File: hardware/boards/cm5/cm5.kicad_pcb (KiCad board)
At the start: 6 copper layers, 64.2 x 85.8 mm, 77 parts, among them J101 10164227-1001A1RLF, J102 10164227-1001A1RLF, J103 BM04B-SRSS-TB, J201 05A20L24P, J401 1054500101, J501 USB4105-GF-A-120, J601 HR911130A, J701 1-2199230-5, M1 CM5, Q401 2N7002, SW501 SKRTLAE010, U301 LM61480RPHR, U401 HD3SS3220RNHR, U402 AP22652W6-7, U403 TPD4E02B04DQAR, U404 TPD4E02B04DQAR, U405 TPD4E05U06DQAR, U501 TPD4E05U06DQAR, U601 TPD4E02B04DQAR, U602 TPD4E02B04DQAR, U701 AP3441SHE-7B

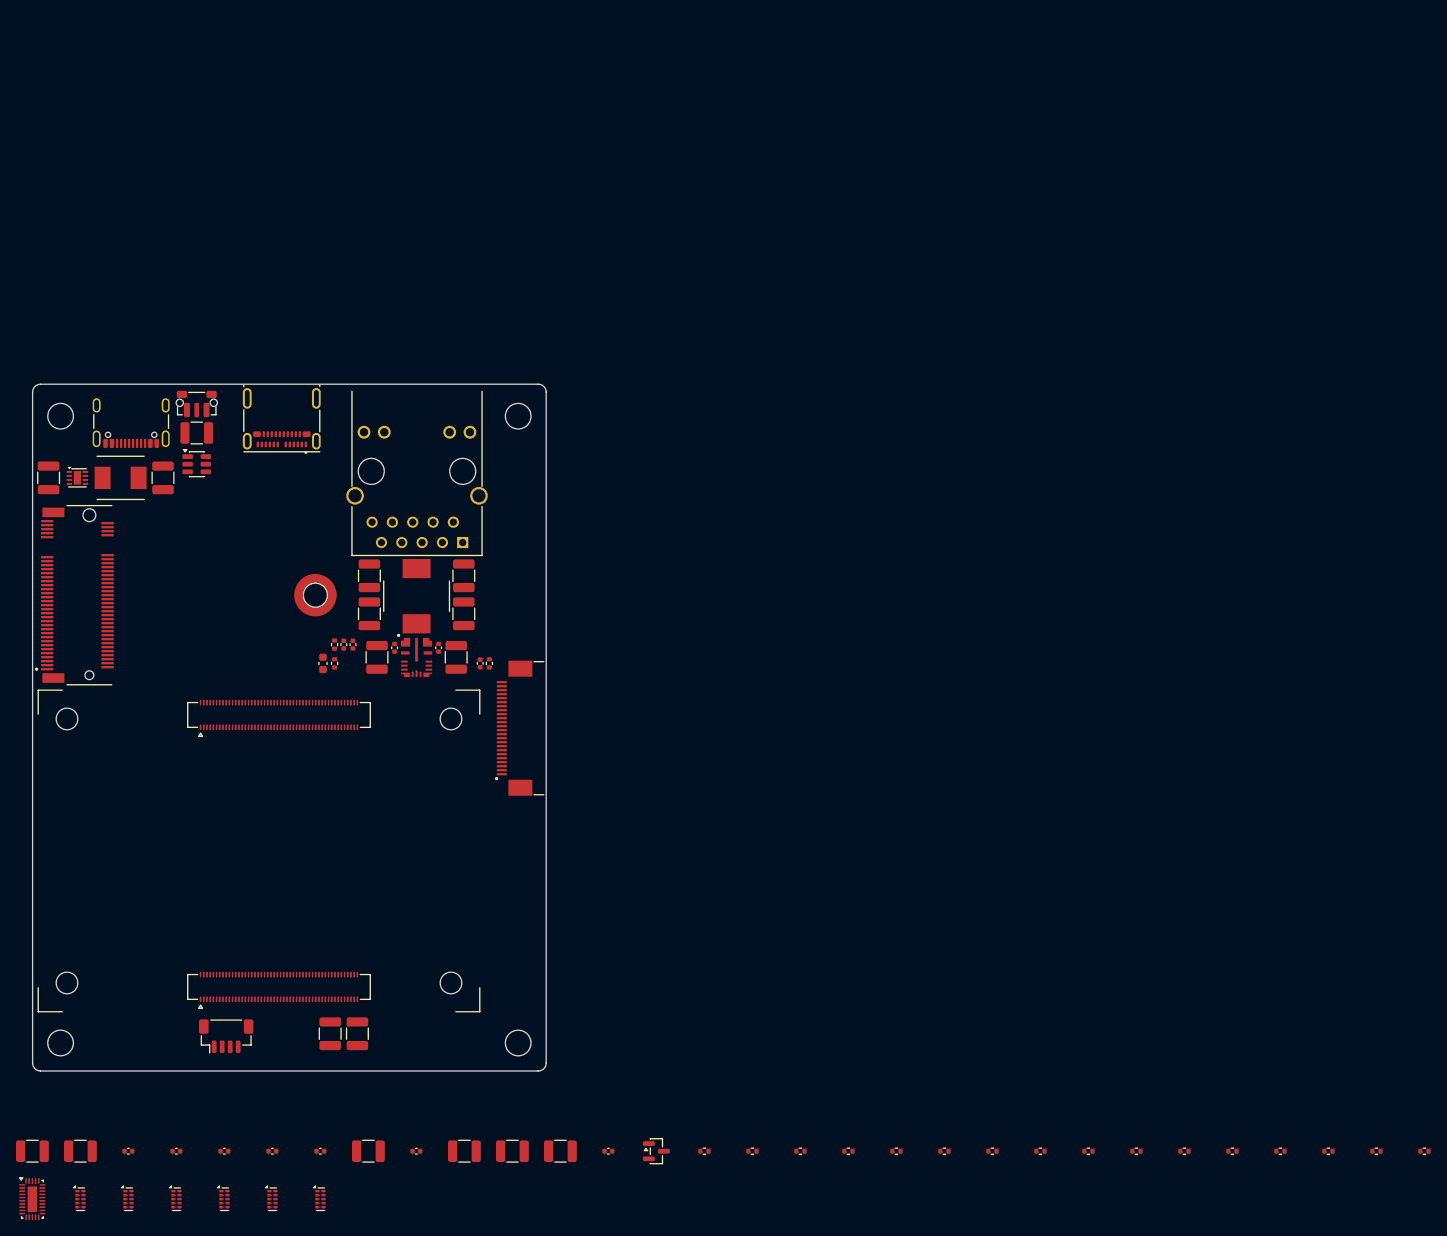
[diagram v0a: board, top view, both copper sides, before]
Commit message: feat(cm5): place the side board around a 2280 beside the turned CM5
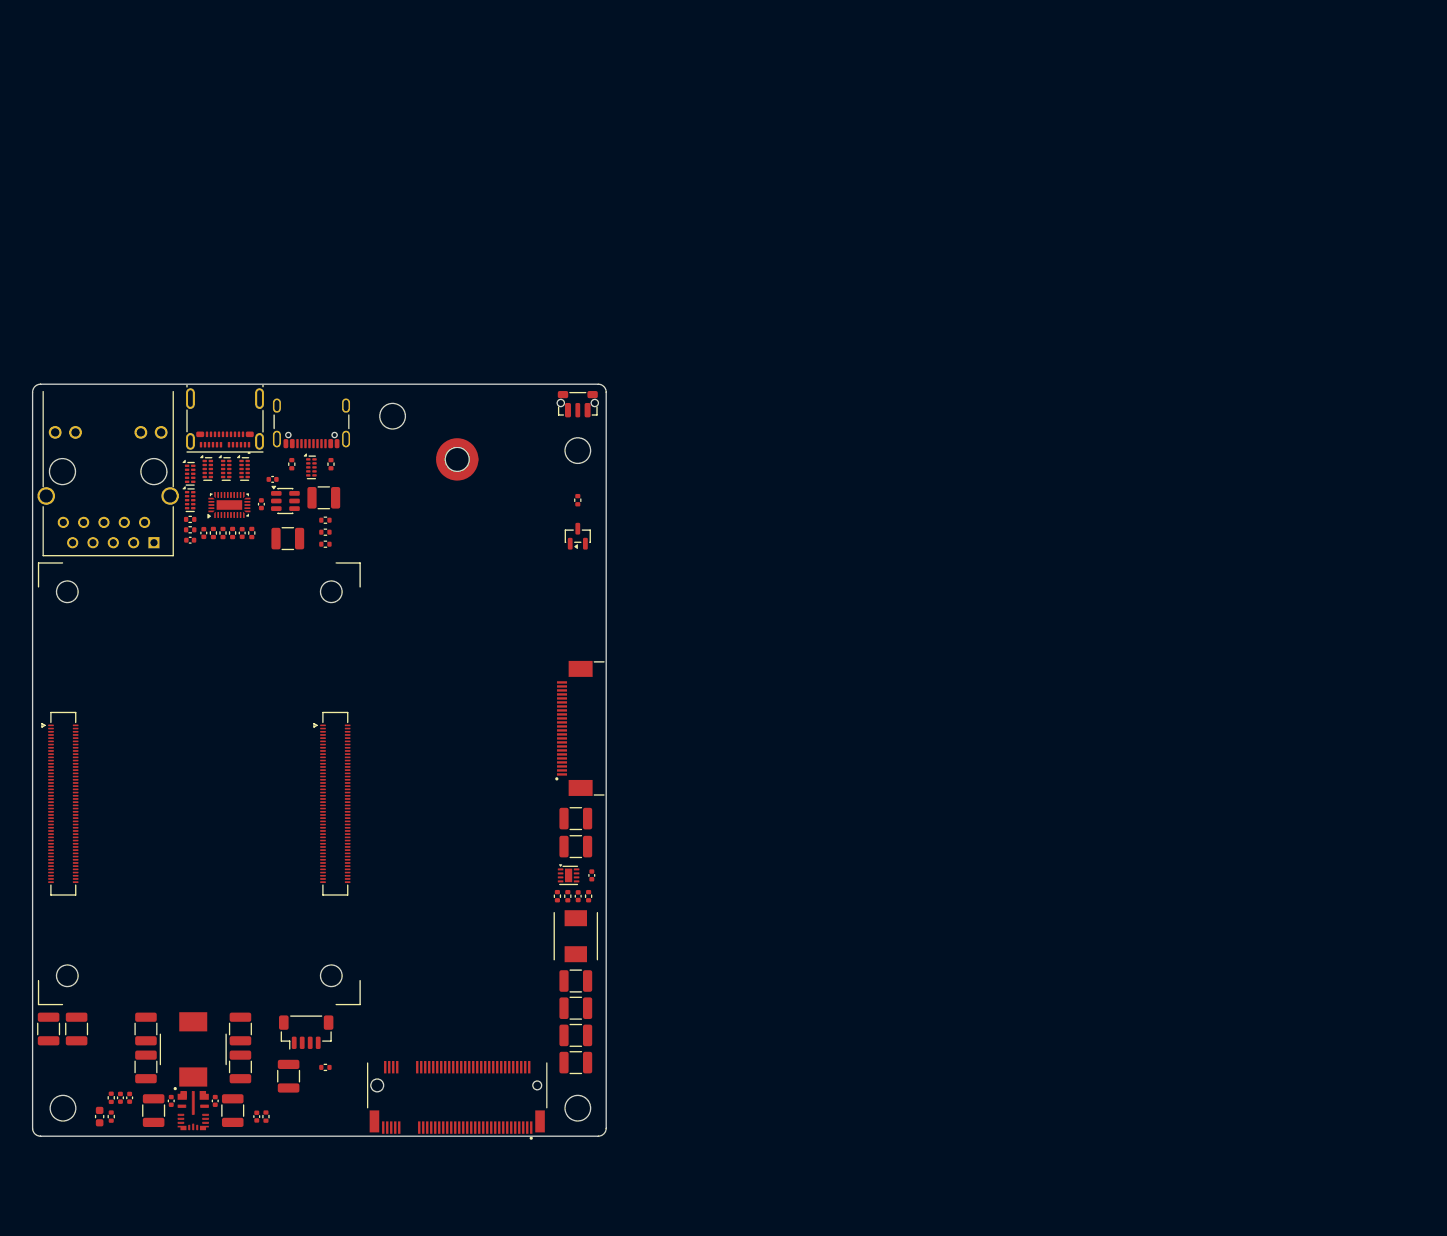
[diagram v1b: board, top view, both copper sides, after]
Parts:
- moved R602 156.9 mm to (119.7, 118.2)
- moved R601 152.3 mm to (119.7, 116.9)
- moved R502 140.8 mm to (132.4, 110.0), turned to 90 degrees
- moved R501 132.3 mm to (137.3, 110.0), turned to 90 degrees
- moved R407 123.8 mm to (136.6, 117.0)
- moved R406 117.2 mm to (136.6, 120.0)
- moved R404 116.0 mm to (127.4, 118.6), turned to 90 degrees
- moved R405 113.7 mm to (136.6, 118.5)
- moved R403 113.4 mm to (125.0, 118.6), turned to 90 degrees
- moved R402 109.9 mm to (123.8, 118.6), turned to 90 degrees
- moved R703 109.2 mm to (169.5, 164.0), turned to 90 degrees
- moved R401 106.6 mm to (122.6, 118.6), turned to 90 degrees
- moved R702 106.0 mm to (166.9, 164.0), turned to 90 degrees
- moved R701 101.5 mm to (165.6, 164.0), turned to 90 degrees
- moved U403 93.6 mm to (126.5, 110.6)
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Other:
- board size 64.2 x 85.8 mm -> 71.7 x 94 mm

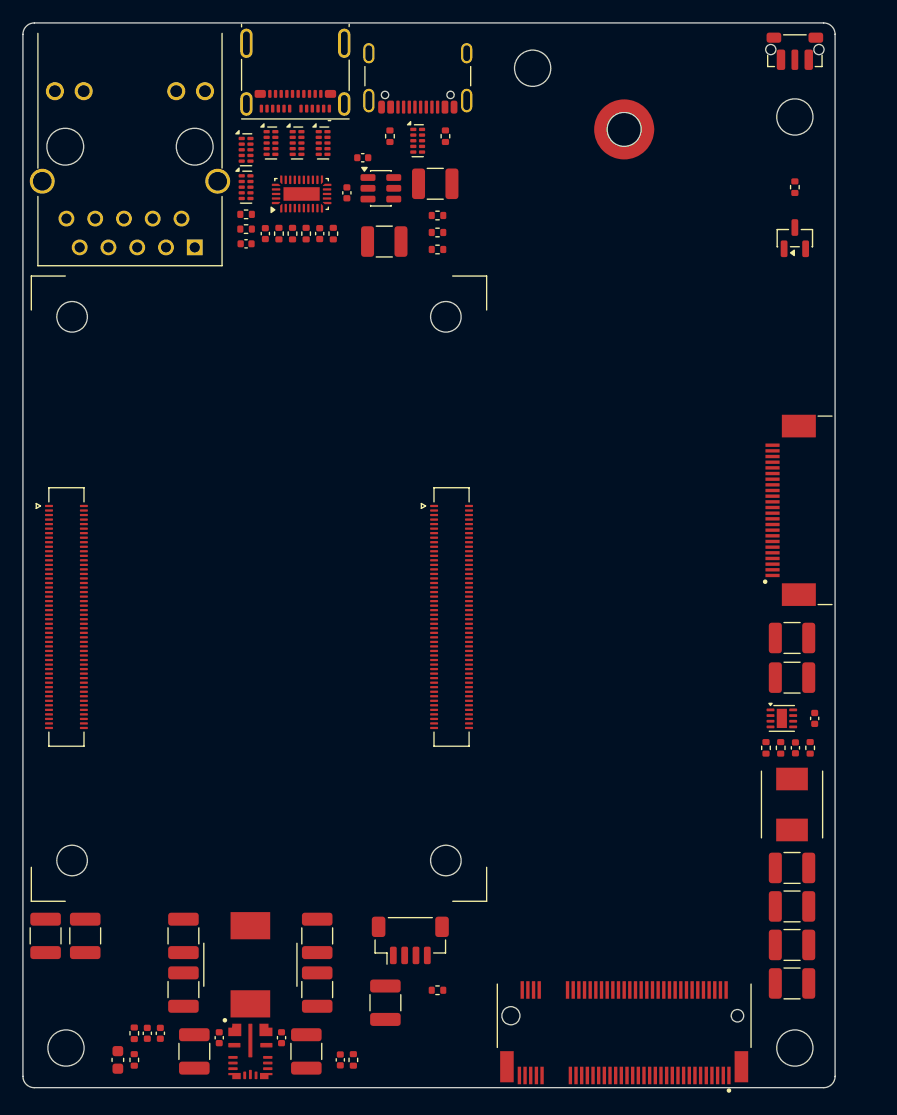
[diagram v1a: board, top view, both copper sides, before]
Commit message: feat(cm5): widen the side board for the CM5 enclosure
The contents move 3.4 mm right so the enclosure's end clip and its travel stop clear the cooler, the RJ45 and C101/C102 at the left edge. The corners take the main board's 3 mm radius, SW501 moves 1 mm in from the rear-right arc, and J501 0.1 mm toward the rear edge so the rear wall keeps 1.0 mm.
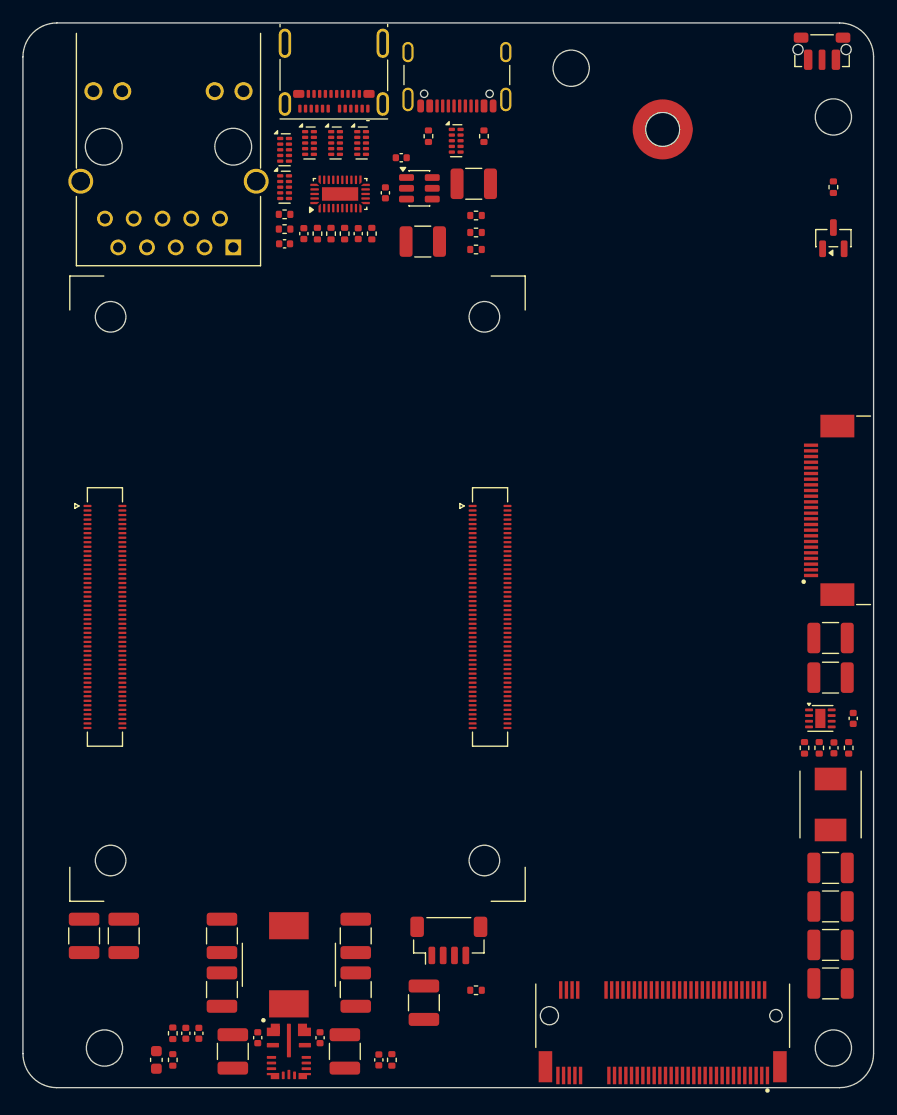
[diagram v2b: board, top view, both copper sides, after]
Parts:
- moved J501 3.45 mm to (138.3, 103.7)
- moved H701 3.40 mm to (156.5, 109.4)
- moved J103 3.40 mm to (137.6, 181.0)
- moved J701 3.40 mm to (156.5, 187.7)
- moved C101 3.40 mm to (105.4, 180.6)
- moved C102 3.40 mm to (108.9, 180.6)
- moved C302 3.40 mm to (118.5, 190.8)
- moved C303 3.40 mm to (126.2, 189.6)
- moved C304 3.40 mm to (120.7, 189.6)
- moved C305 3.40 mm to (115.5, 189.2)
- moved C306 3.40 mm to (111.8, 191.6)
- moved C312 3.40 mm to (135.4, 186.5)
- moved C401 3.40 mm to (139.8, 114.2)
- moved C404 3.40 mm to (132.0, 115.0)
- moved C405 3.40 mm to (135.3, 119.3)
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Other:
- board size 71.7 x 94 mm -> 75.1 x 94 mm

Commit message: feat(cm5): take the side link on a vertical FH12 at the right edge
J201 becomes a Hirose FH12-24S-0.5SVA(54), contacts toward the right edge with its lands 0.3 mm from it, pin 1 at the front end; main pin n still meets J201 pin 25 - n.
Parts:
- J201: value 05A20L24P -> FH12-24S-0.5SVA(54); footprint Iasis:HanElectricity_05A20L24P -> Iasis:Hirose_FH12-24S-0.5SVA_1x24-1MP_P0.50mm_Vertical
- moved J201 1.81 mm to (172.6, 143.0), turned to -90 degrees

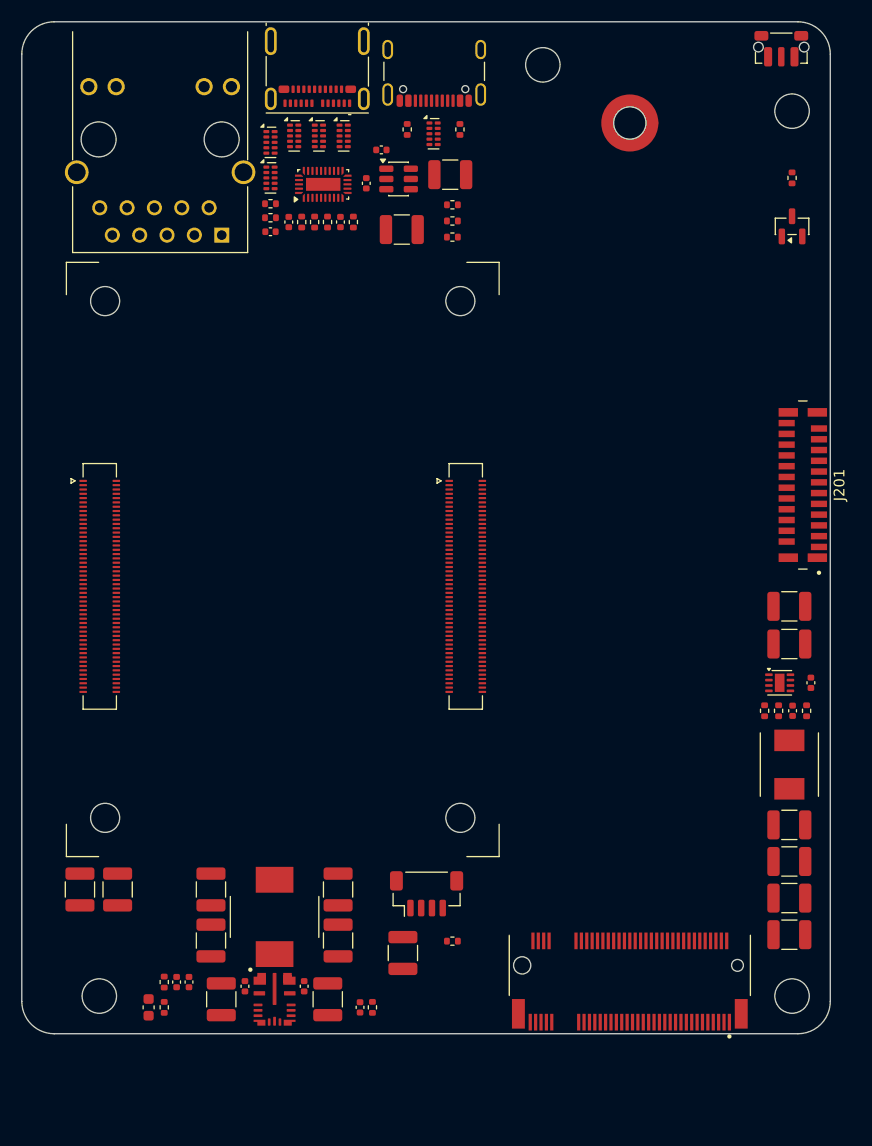
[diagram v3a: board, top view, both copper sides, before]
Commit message: feat(cm5): add the status light and short M.2 standoffs, space the rear ports
The side board grows to the main board's 102 mm depth, so the status light sits at the enclosure's front wall and the 2280 standoff clears the rear strip. RJ45, accessory and service USB-C now have even gaps with H4 between the USB-Cs and nRPIBOOT beside the service port. The status light is the main board's SK6812SIDE-A behind an SN74AHCT1G125 on GPIO10; H702 and H703 take 2230 and 2242 drives. The accessory ESD follows the main board's port cell, with TX1/TX2 polarity swapped at the receptacle as there.
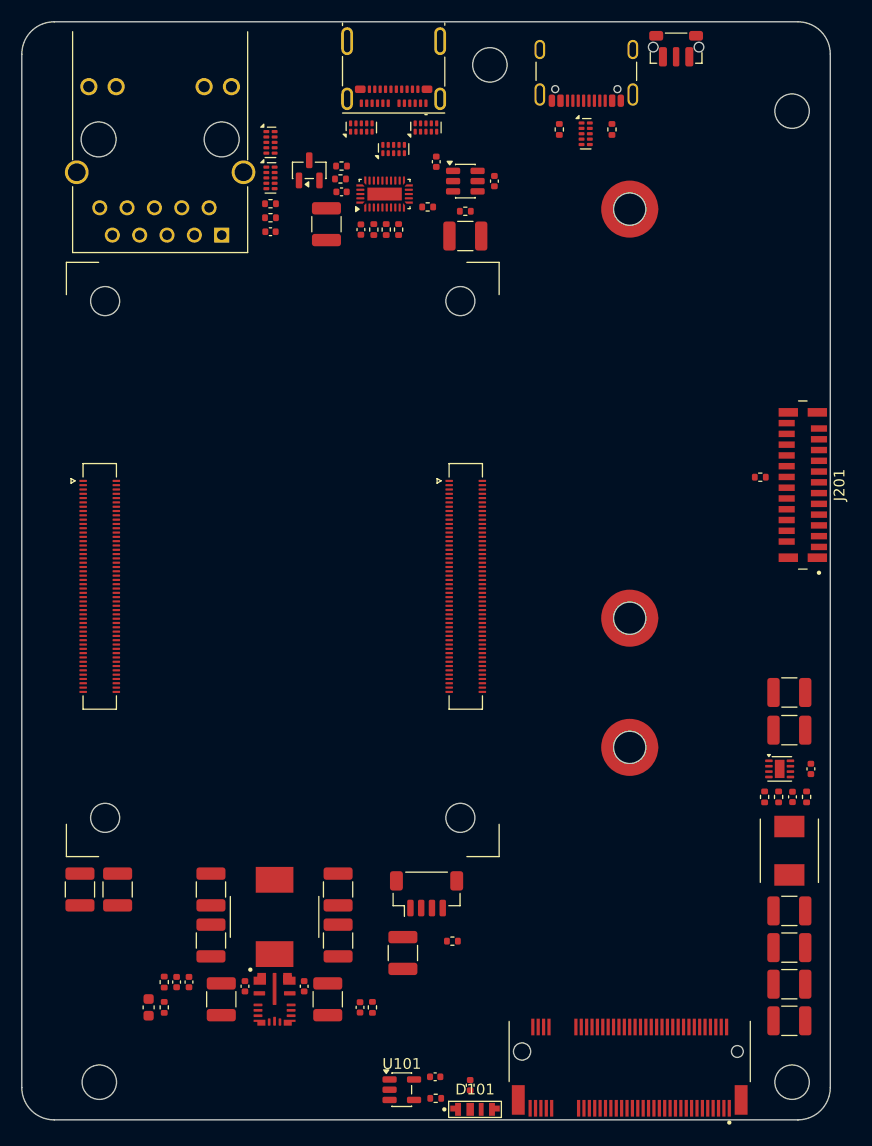
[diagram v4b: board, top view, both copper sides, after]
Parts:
- added C103: 100n, Capacitor_SMD:C_0402_1005Metric, F.Cu at (141.7, 198.8)
- added C104: 100n, Capacitor_SMD:C_0402_1005Metric, F.Cu at (138.4, 198.0)
- added D101: SK6812SIDE-A, Iasis:OPSCO_SK6812SIDE-A, F.Cu at (142.1, 201.0)
- added H702: 9774025243R, Mounting_Wuerth:Mounting_Wuerth_WA-SMSI-M2_H2.5mm_9774025243, F.Cu at (156.5, 167.4)
- added H703: 9774025243R, Mounting_Wuerth:Mounting_Wuerth_WA-SMSI-M2_H2.5mm_9774025243, F.Cu at (156.5, 155.4)
- added R102: 33, Resistor_SMD:R_0402_1005Metric, F.Cu at (138.4, 200.0)
- added U101: SN74AHCT1G125DBVR, Package_TO_SOT_SMD:SOT-23-5, F.Cu at (135.3, 199.2)
- moved Q401 45.2 mm to (126.7, 113.8)
- moved R201 28.0 mm to (168.6, 142.3), turned to 0 degrees
- moved J501 14.1 mm to (152.4, 103.7)
- moved R502 14.1 mm to (149.9, 110.0)
- moved U501 14.1 mm to (152.4, 110.4)
- moved R501 14.1 mm to (154.8, 110.0)
- moved C401 12.4 mm to (128.3, 118.8), turned to 90 degrees
- moved R406 12.2 mm to (129.7, 113.4)
- moved R405 11.1 mm to (129.6, 114.6)
- moved C406 10.9 mm to (143.9, 114.8), turned to 90 degrees
- moved SW501 9.77 mm to (160.8, 102.3)
- moved C708 8.00 mm to (171.6, 172.0)
- moved H701 8.00 mm to (156.5, 117.4)
- moved J701 8.00 mm to (156.5, 195.7)
- moved C701 8.00 mm to (171.3, 162.3)
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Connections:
- J101 pad 44: unconnected-(J101-GPIO10-Pad44) -> /Compute module/LED_DATA
- J401 pad A2: /Accessory port/TX1_P -> /Accessory port/TX1_N
- J401 pad A3: /Accessory port/TX1_N -> /Accessory port/TX1_P
- J401 pad B2: /Accessory port/TX2_P -> /Accessory port/TX2_N
- J401 pad B3: /Accessory port/TX2_N -> /Accessory port/TX2_P
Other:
- board size 75.1 x 94 mm -> 75.1 x 102 mm
